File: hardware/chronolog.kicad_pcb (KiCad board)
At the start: 2 copper layers, 120 x 90 mm, 96 parts, among them J1 DC-005-5A-2.0, J2 B4B-XH-A, J3 B-2100S04P-A110, J4 U254-051N-4BH806, Q1 BSS138, Q2 BSS138, Q3 BC817-40LT1G, U1 AP63205WU-7, U2 STM32F072CBT6, U3 AP2114H-3.3TRG1, U4 USBLC6-2SC6, U5 W25Q32JVSNIQ, U6 LM75BD, U7 ESP-01, U8 WC1602A, U9 PCF8574T, Y1 32.768kHz

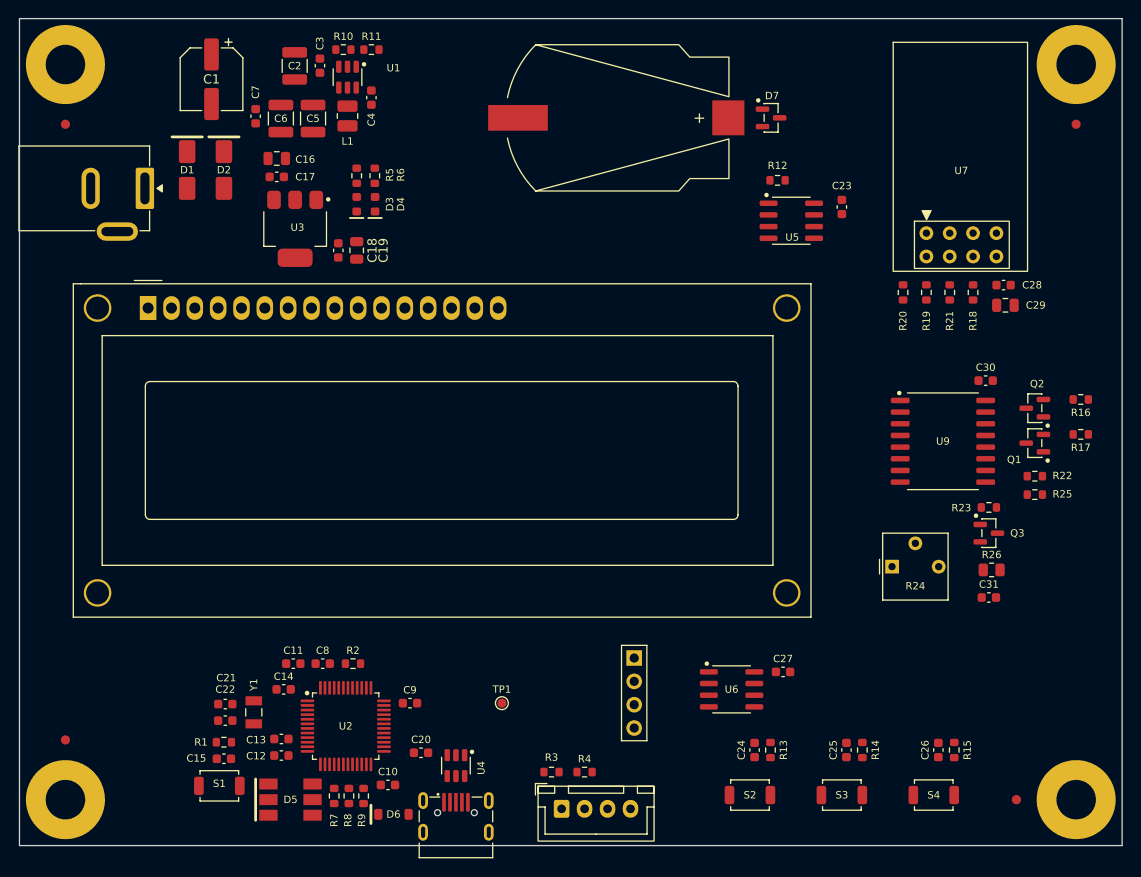
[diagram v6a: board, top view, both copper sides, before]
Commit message: hardware(feat): resize the board and reorder circuits
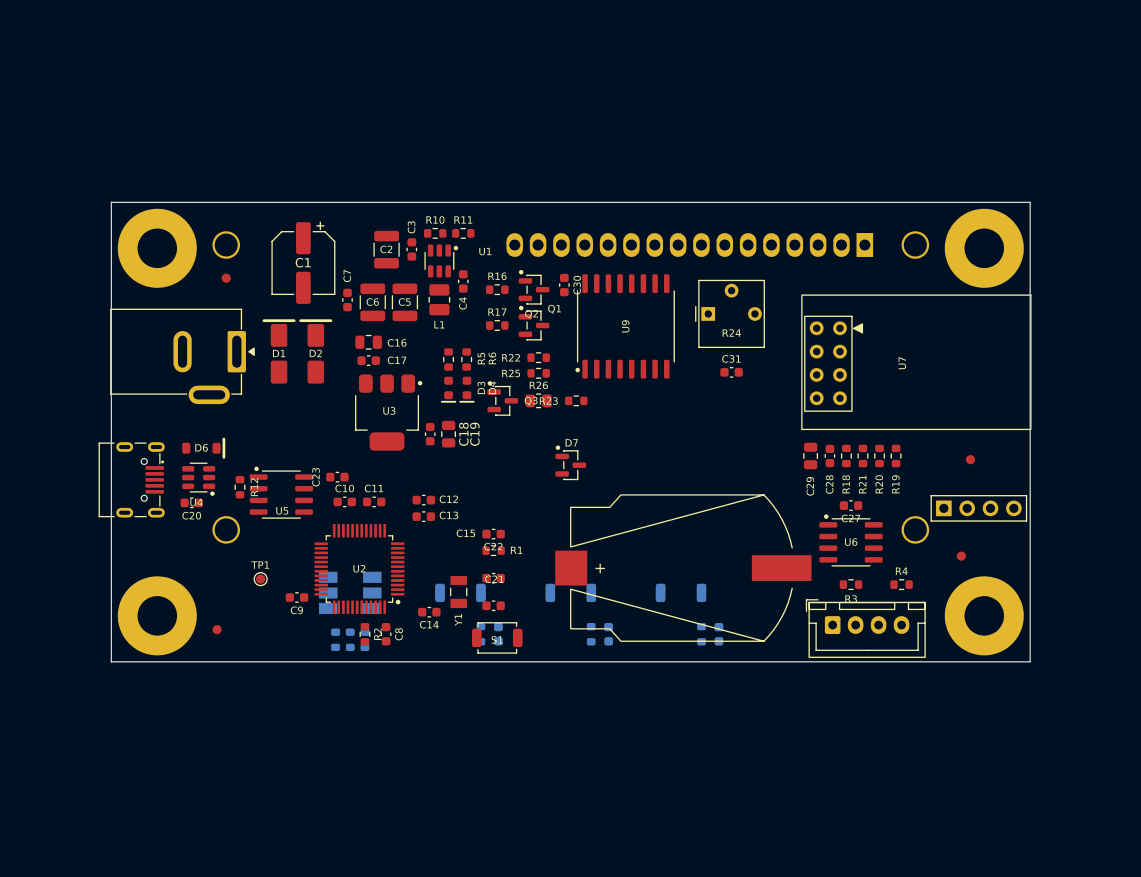
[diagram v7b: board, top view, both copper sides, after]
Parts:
- C24, C25, C26, D5, R13, R14, R15, R7, R8, R9, S2, S3, S4, U8: moved to B.Cu
- moved U8 78.3 mm to (180.5, 84.6), turned to 180 degrees
- moved R12 67.4 mm to (112.5, 111.0), turned to 90 degrees
- moved R16 64.6 mm to (140.5, 89.5), turned to 0 degrees
- moved R17 64.6 mm to (140.5, 93.4), turned to 0 degrees
- moved U5 63.0 mm to (117.0, 111.8)
- moved C23 62.3 mm to (123.1, 109.9), turned to 0 degrees
- moved Q2 56.0 mm to (144.5, 89.5), turned to 0 degrees
- moved S4 56.0 mm to (136.5, 122.5)
- moved Q1 56.0 mm to (144.5, 93.4), turned to 0 degrees
- moved R25 55.6 mm to (145.0, 98.6), turned to 0 degrees
- moved R22 55.5 mm to (145.0, 96.9), turned to 0 degrees
- moved Q3 54.8 mm to (141.1, 101.6)
- moved R15 53.0 mm to (138.7, 127.0), turned to 90 degrees
- moved R26 52.6 mm to (145.0, 101.6)
- moved J4 51.9 mm to (100.5, 110.2), turned to -90 degrees
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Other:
- board size 120 x 90 mm -> 100 x 50 mm
- board text added: "DC SUPPLY 5V + LDO 3V3"
- board text added: "MCU STM32 + NOR FLASH"
- board text added: "RTC BATTERY (BT1)"
- board text added: "TEMP (LM75) + SWD/UART"
- board text added: "USB IN"
- board text added: "[BOTTOM] BUTTONS + RGB LED"
- board text added: "[BOTTOM] LCD 16x2 (WC1602A)"
- board text removed: "BUTTONS + TEMP SENSOR (LM75)"
- board text removed: "DC SUPPLY 5V + LDO 3V3 (AP63205 / AP2114)"
- board text removed: "LCD 16x2 (WC1602A)"
- board text removed: "MCU STM32 + USB + SWD/UART + LED"
- board text removed: "RTC + NOR FLASH (BT1 / W25Q32)"

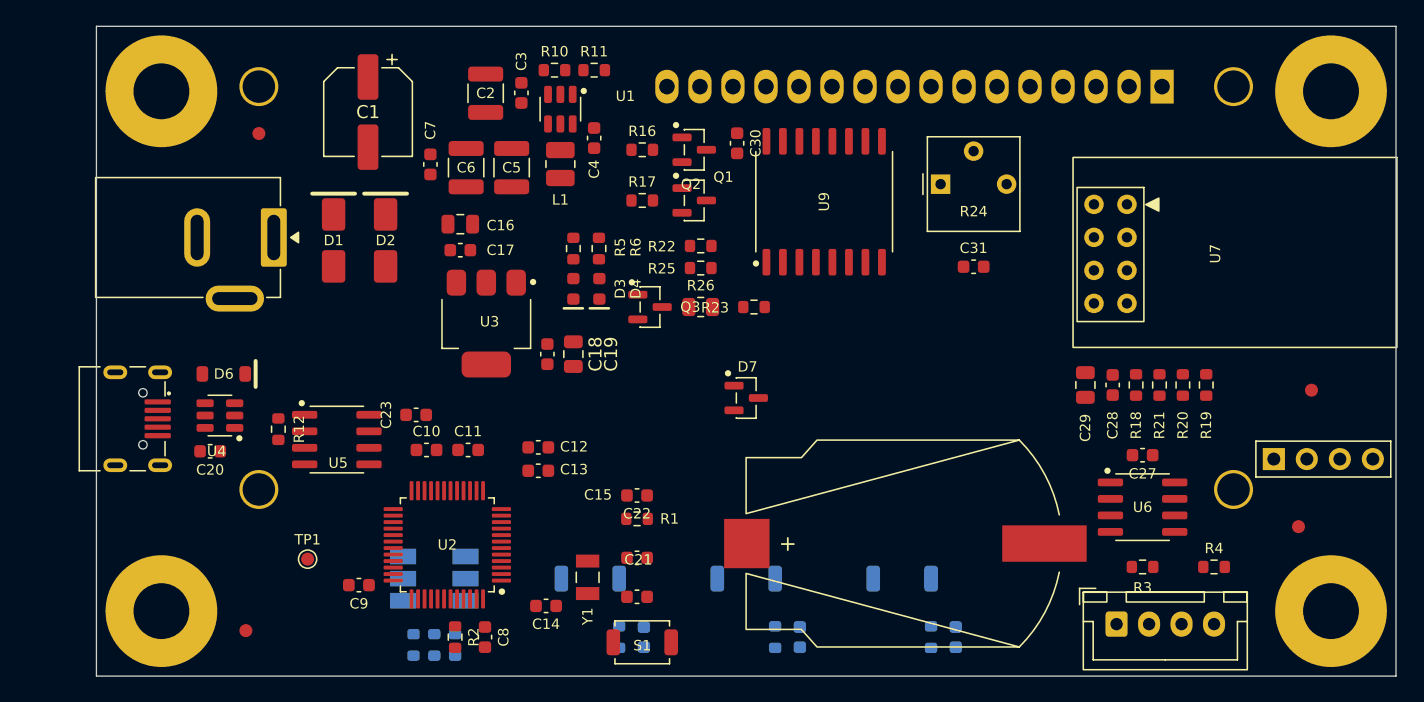
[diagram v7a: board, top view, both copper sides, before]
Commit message: hardware(feat): complete pcb placement, closes #15
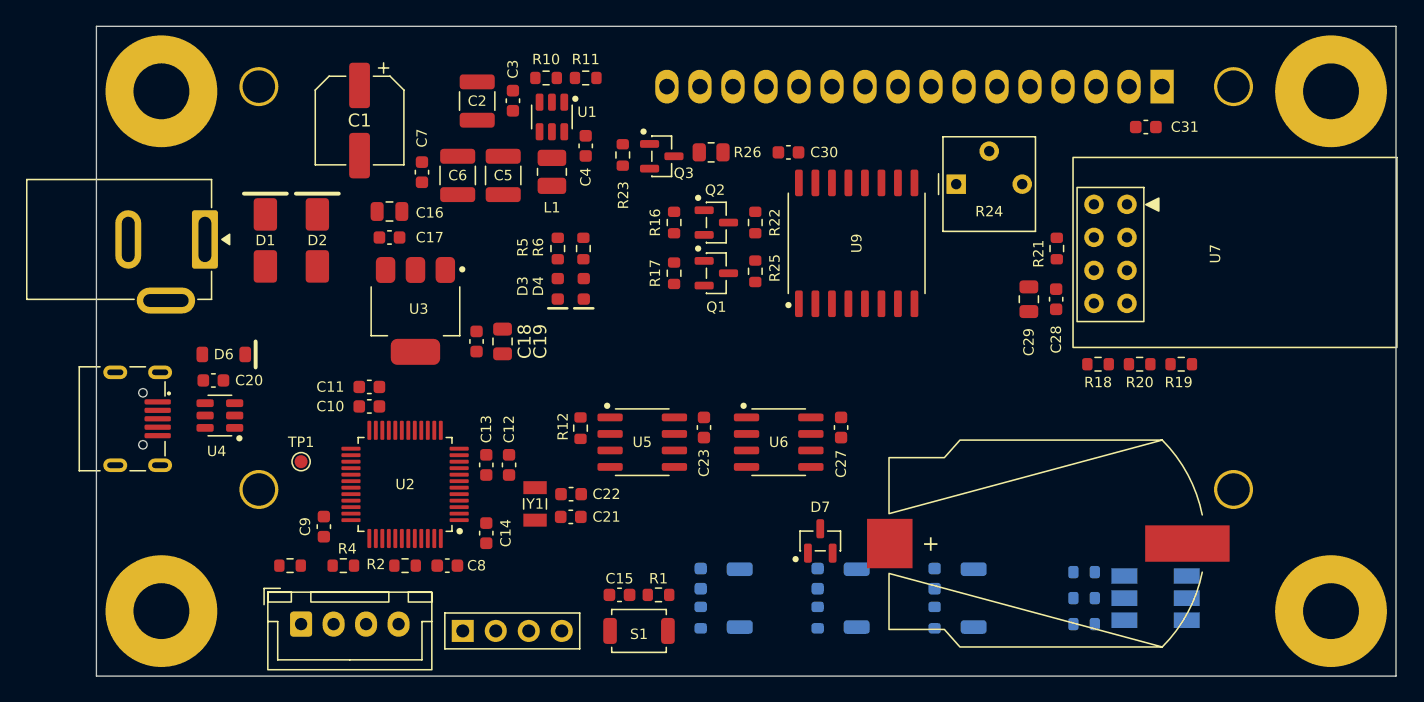
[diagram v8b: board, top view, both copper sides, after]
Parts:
- removed FID1, FID2, FID3, FID4: 1.0P-2.0M, 12_mechanical:Fiducial_1mm_Mask2mm
- moved R4 67.0 mm to (117.5, 121.5), turned to 180 degrees
- moved R3 65.6 mm to (113.4, 121.5), turned to 180 degrees
- moved J3 63.8 mm to (126.7, 126.5)
- moved J2 62.8 mm to (114.2, 126.0)
- moved D5 55.5 mm to (180.0, 124.0), turned to 180 degrees
- moved R7 51.7 mm to (174.5, 124.0), turned to 180 degrees
- moved R8 50.0 mm to (174.5, 126.0), turned to 0 degrees
- moved R9 48.7 mm to (174.5, 122.0), turned to 180 degrees
- moved U6 28.4 mm to (151.0, 112.0)
- moved U5 23.5 mm to (140.5, 112.0)
- moved C27 23.3 mm to (155.8, 110.9), turned to -90 degrees
- moved R12 23.3 mm to (135.8, 110.9), turned to -90 degrees
- moved C23 22.2 mm to (145.2, 110.9), turned to -90 degrees
- moved C31 17.1 mm to (179.2, 87.8)
- moved R23 15.5 mm to (139.0, 89.9), turned to 90 degrees
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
